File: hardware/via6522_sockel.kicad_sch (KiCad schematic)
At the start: 3 parts, among them IC2 VIA6522, P1 VIA_PIN_1-20, P2 VIA_PIN_21-40

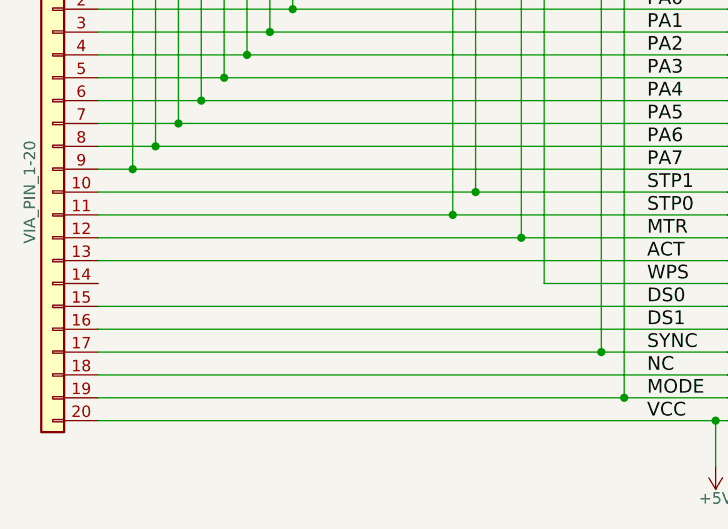
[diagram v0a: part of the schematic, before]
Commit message: first attempt for better WPS handling
a)disconnect WPS from Pico
b)still connect 1541-mainboard WPS with VIA on 1541-rePico
c)connect Pico-WPS output to input of 1541-mainboard
input of photo-sensor (=1541-II -> CN4,pin3)
d)invert Pico-output as 1541-board does the inversion again
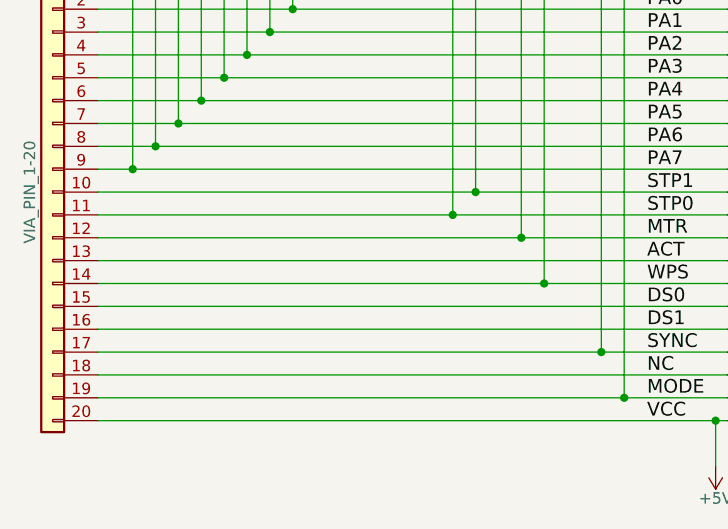
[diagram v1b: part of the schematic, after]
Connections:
- net WPS: now also P1.14 (Pin_14)
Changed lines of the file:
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@@
 	(title_block
 		(title "1541-rePico")
-		(date "2026-02-11")
-		(rev "1.2")
+		(date "2026-02-12")
+		(rev "1.21")
 	)
 	(junction
@@
 	)
 	(junction
+		(at 128.27 101.6)
+		(diameter 0)
+		(color 0 0 0 0)
+	)
+	(junction
 		(at 137.16 114.3)
 		(diameter 0)
@@
 		(pts
 			(xy 177.8 101.6) (xy 222.25 101.6)
+		)
+		(stroke
+			(width 0)
+			(type default)
+		)
+	)
+	(wire
+		(pts
+			(xy 78.74 101.6) (xy 128.27 101.6)
 		)
 		(stroke
@@
 		(on_board yes)
 		(dnp no)
-		(property "Reference" "#PWR025"
+		(property "Reference" "#PWR?"
 			(at 147.32 118.11 0)
 			(effects
@@
 				(path "/7c37ffbe-d8d1-4c30-ad42-fd3ef959e14d/00000000-0000-0000-0000-000055f9b22c"
 					(reference "#PWR025")
+					(unit 1)
+				)
+			)
+			(project "via6522_sockel"
+				(path "/c37ad323-a4c8-4cb0-847b-5650f1f69eb4"
+					(reference "#PWR?")
 					(unit 1)
 				)
@@
 		(on_board yes)
 		(dnp no)
-		(property "Reference" "P2"
+		(property "Reference" "P?"
 			(at 227.33 120.65 0)
 			(effects
@@
 				(path "/7c37ffbe-d8d1-4c30-ad42-fd3ef959e14d/00000000-0000-0000-0000-000055f9b22c"
 					(reference "P2")
+					(unit 1)
+				)
+			)
+			(project "via6522_sockel"
+				(path "/c37ad323-a4c8-4cb0-847b-5650f1f69eb4"
+					(reference "P?")
 					(unit 1)
 				)
@@
 		(on_board yes)
 		(dnp no)
-		(property "Reference" "P1"
+		(property "Reference" "P?"
 			(at 73.66 64.77 0)
 			(effects
@@
 				(path "/7c37ffbe-d8d1-4c30-ad42-fd3ef959e14d/00000000-0000-0000-0000-000055f9b22c"
 					(reference "P1")
+					(unit 1)
+				)
+			)
+			(project "via6522_sockel"
+				(path "/c37ad323-a4c8-4cb0-847b-5650f1f69eb4"
+					(reference "P?")
 					(unit 1)
 				)
@@
 		(on_board yes)
 		(dnp no)
-		(property "Reference" "#PWR024"
+		(property "Reference" "#PWR?"
 			(at 147.32 55.88 0)
 			(effects
@@
 				(path "/7c37ffbe-d8d1-4c30-ad42-fd3ef959e14d/00000000-0000-0000-0000-000055f9b22c"
 					(reference "#PWR024")
+					(unit 1)
+				)
+			)
+			(project "via6522_sockel"
+				(path "/c37ad323-a4c8-4cb0-847b-5650f1f69eb4"
+					(reference "#PWR?")
 					(unit 1)
 				)
@@
 		(on_board yes)
 		(dnp no)
-		(property "Reference" "IC2"
+		(property "Reference" "IC?"
 			(at 163.195 61.2902 0)
 			(effects
@@
 				)
 			)
-		)
-	)
+			(project "via6522_sockel"
+				(path "/c37ad323-a4c8-4cb0-847b-5650f1f69eb4"
+					(reference "IC?")
+					(unit 1)
+				)
+			)
+		)
+	)
+	(sheet_instances
+		(path "/"
+			(page "1")
+		)
+	)
+	(embedded_fonts no)
 )
